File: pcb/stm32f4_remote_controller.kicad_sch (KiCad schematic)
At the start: 0 parts

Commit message: pcb: add source supply
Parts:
- added C1, C2, C3, C4, C5, C7: 100n, symbol Device:C
- added C6: 10u, symbol Device:C
- added C8, C9: 20p, symbol Device:C
- added J1: Conn_01x04_Pin, symbol Connector:Conn_01x04_Pin
- added U1: STM32F401CCU6, Package_DFN_QFN:QFN-48-1EP_7x7mm_P0.5mm_EP5.6x5.6mm, symbol MCU_ST_STM32F4:STM32F401CCUx
- added Y1: 8Mhz, symbol Device:Crystal_GND24
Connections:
- new net +STEP_UP_3.3V: C1.1, C2.1, C3.1, C4.1, C5.1, C6.1, J1.1 (Pin_1), U1.1 (VBAT), U1.24 (VDD), U1.36 (VDD), U1.48 (VDD)
- new net GND: C1.2, C2.2, C3.2, C4.2, C5.2, C6.2, C7.2, C8.2, C9.2, J1.4 (Pin_4), U1.23 (VSS), U1.35 (VSS), U1.44 (BOOT0), U1.47 (VSS), U1.49 (VSS), U1.8 (VSSA), Y1.2, Y1.4
- new net HSE_IN: C9.1, U1.5 (PH0), Y1.1
- new net HSE_OUT: C8.1, U1.6 (PH1), Y1.3
- new net NRST: C7.1, U1.7 (NRST)
- new net SWCLK: J1.3 (Pin_3), U1.37 (PA14)
- new net SWDIO: J1.2 (Pin_2), U1.34 (PA13)

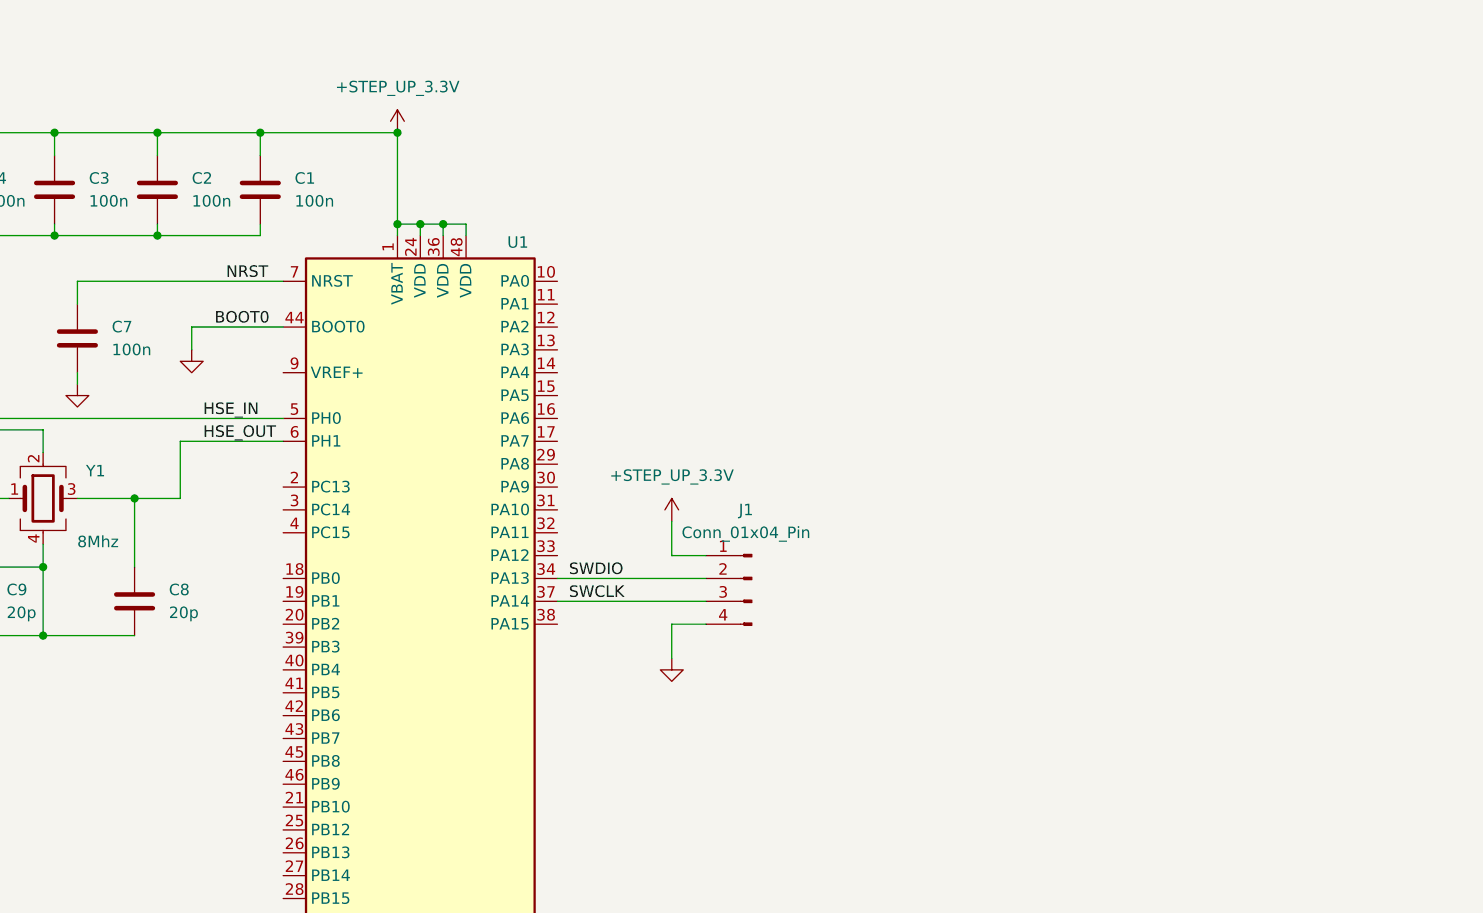
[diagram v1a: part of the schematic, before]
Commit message: pcb: add oled to sch
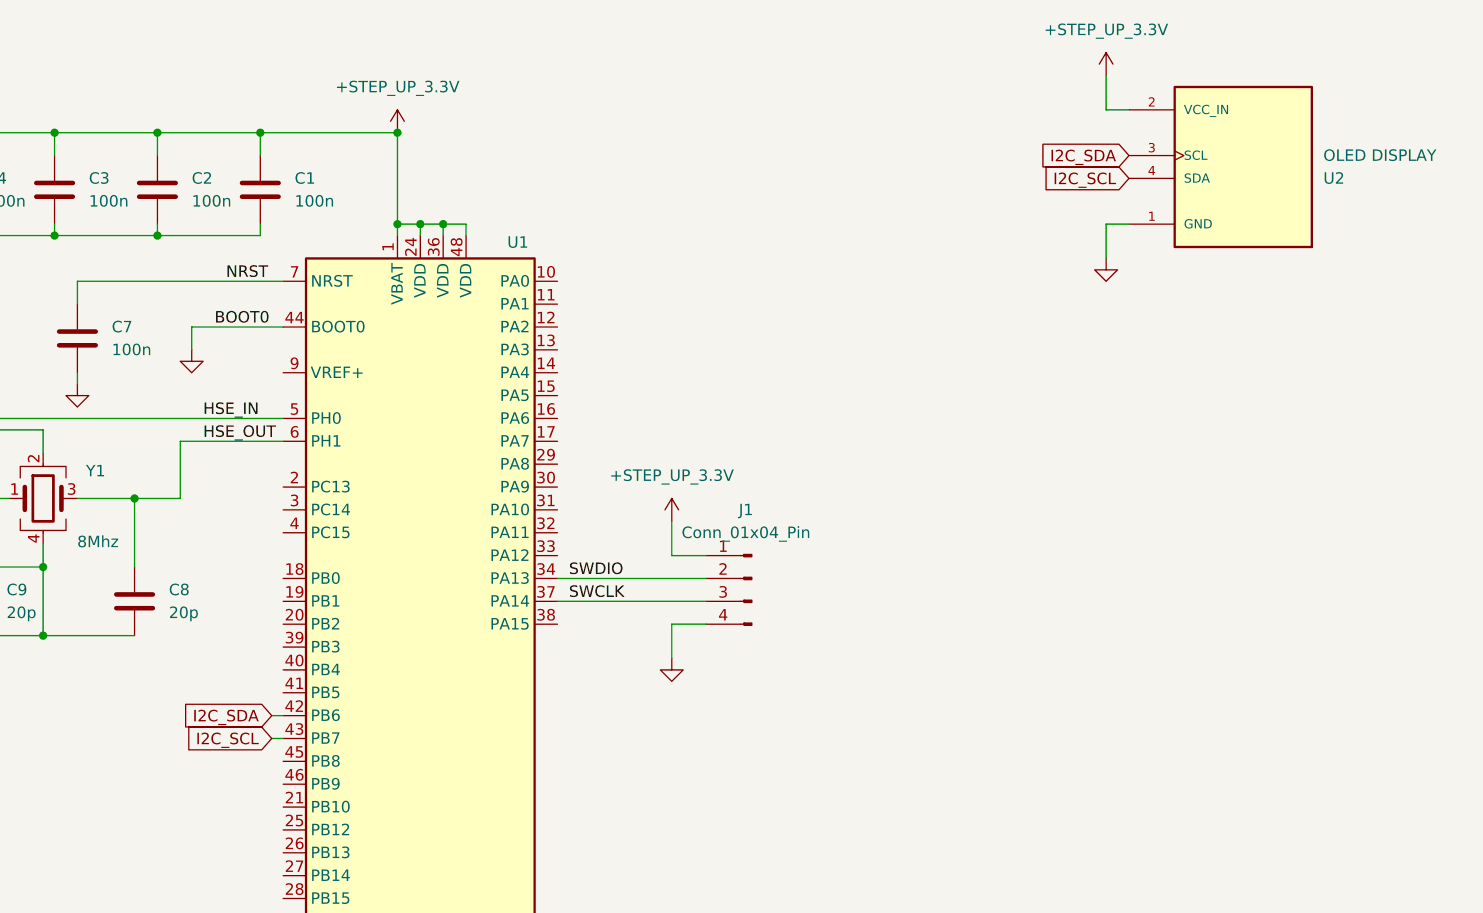
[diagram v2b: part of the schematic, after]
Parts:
- added U2: OLED DISPLAY, DM-OLED096-636:MODULE_DM-OLED096-636, symbol DM-OLED096-636:DM-OLED096-636
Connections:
- net +STEP_UP_3.3V: now also U2.2 (VCC_IN)
- net GND: now also U2.1 (GND)
- net I2C_SDA: now reaches U1.42 (PB6)
- net I2C_SDA: now also U2.3 (SCL)
- net I2C_SCL: now reaches U1.43 (PB7)
- net I2C_SCL: now also U2.4 (SDA)

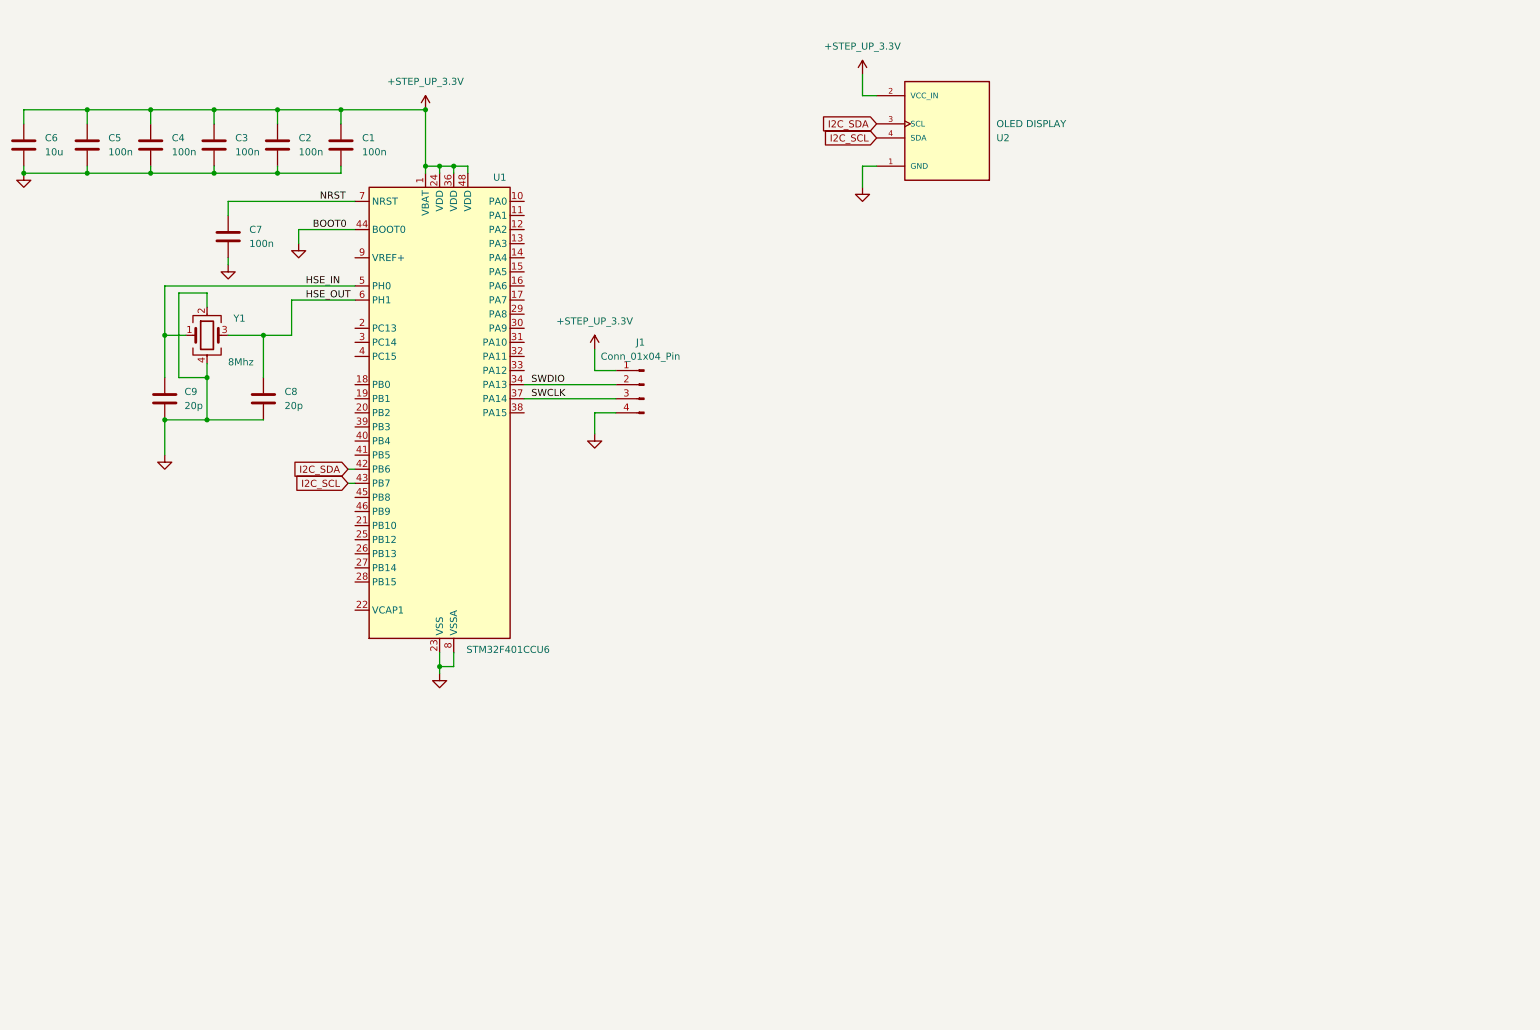
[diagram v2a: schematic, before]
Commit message: pcb: add hm-10 sch
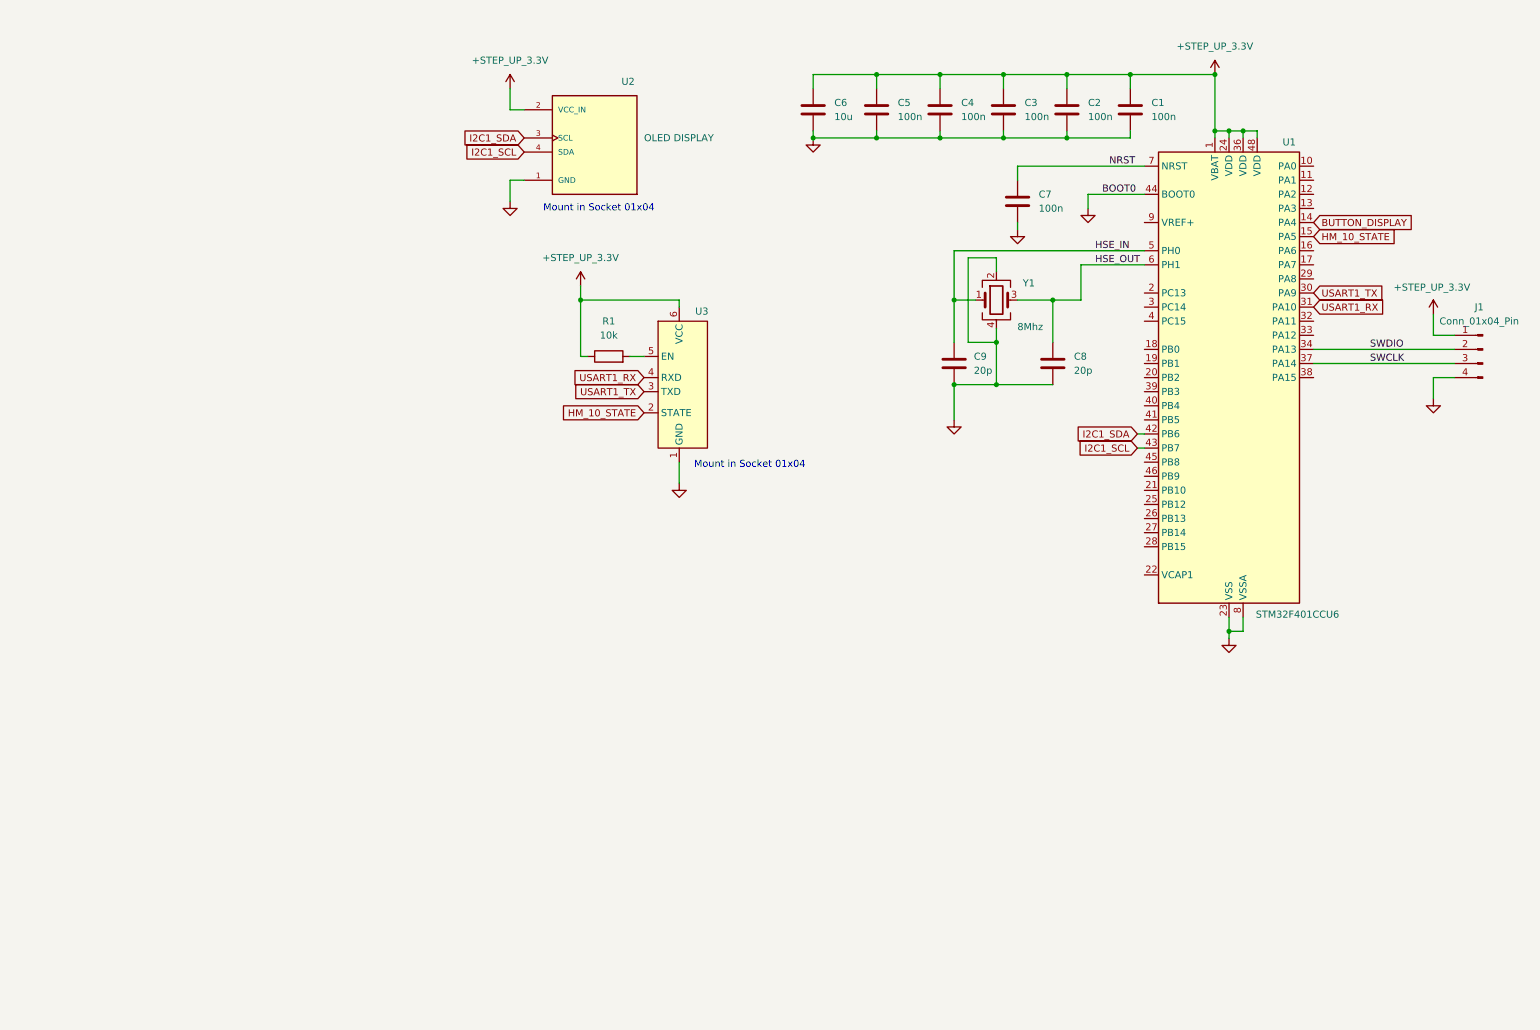
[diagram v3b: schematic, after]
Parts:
- added R1: 10k, symbol Device:R
- added U3: ~, symbol hm-10:hm-10
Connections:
- net +STEP_UP_3.3V: now also R1.1, U3.6 (VCC)
- net GND: now also U3.1 (GND)
- net BUTTON_DISPLAY: now reaches U1.14 (PA4)
- net HM_10_STATE: now reaches U1.15 (PA5)
- net HM_10_STATE: now also U3.2 (STATE)
- net USART1_TX: now reaches U1.30 (PA9)
- net USART1_TX: now also U3.3 (TXD)
- net USART1_RX: now reaches U1.31 (PA10)
- net USART1_RX: now also U3.4 (RXD)
- net I2C_SCL renamed I2C1_SCL
- net I2C_SDA renamed I2C1_SDA
- new net: R1.2, U3.5 (EN)
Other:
- note added: "Mount in Socket 01x04"
- moved on the sheet: C1, C2, C3, C4, C5, C6, C7, C8, C9, J1, U1, U2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

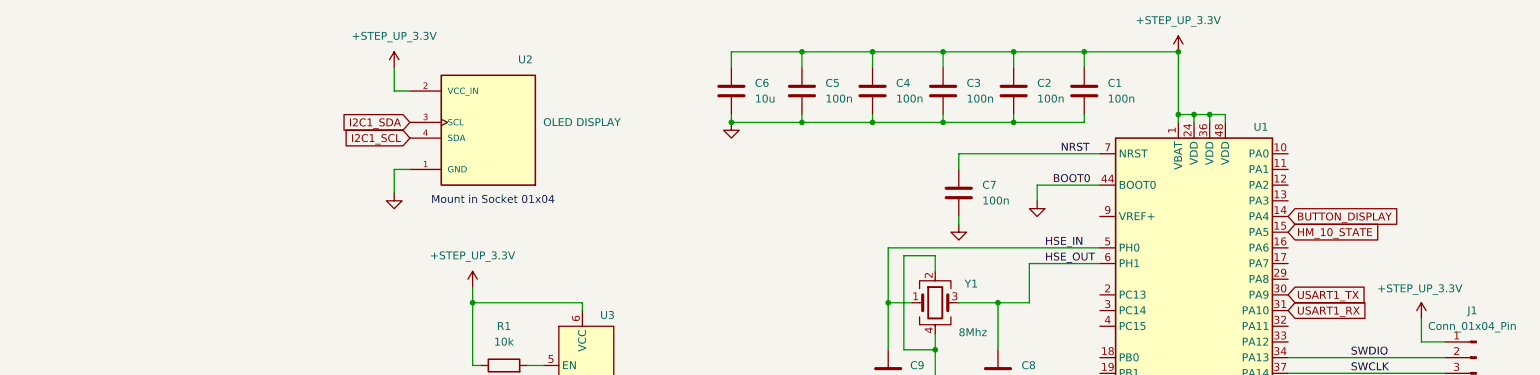
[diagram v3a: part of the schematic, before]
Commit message: pcb: add button debounce circuit
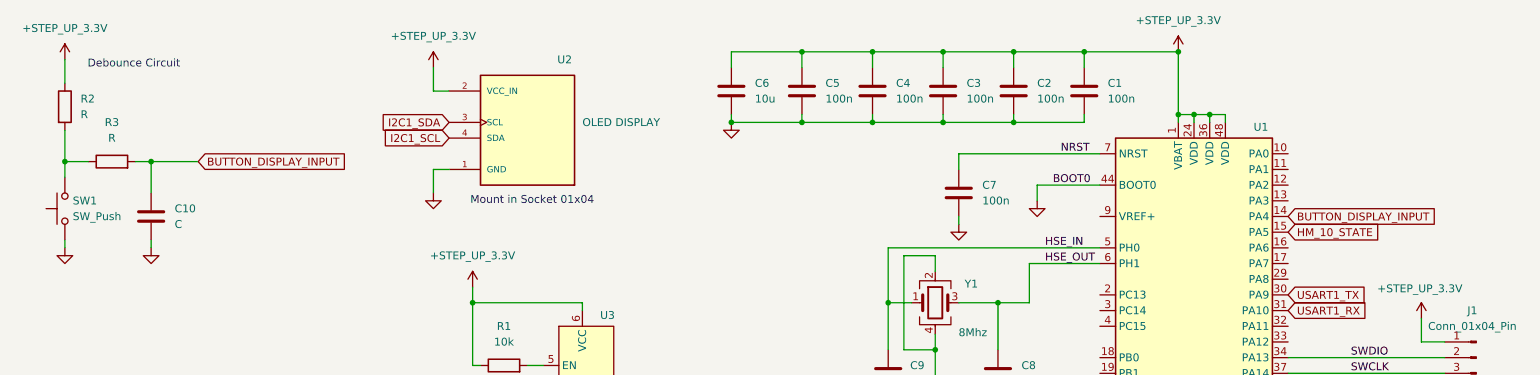
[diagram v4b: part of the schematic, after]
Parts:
- added C10: C, symbol Device:C
- added R2, R3: R, symbol Device:R
- added SW1: SW_Push, symbol Switch:SW_Push
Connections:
- net +STEP_UP_3.3V: now also R2.1
- net GND: now also C10.2, SW1.1
- net BUTTON_DISPLAY renamed BUTTON_DISPLAY_INPUT
- net BUTTON_DISPLAY_INPUT: now also C10.1, R3.2
- new net: R2.2, R3.1, SW1.2
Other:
- note added: "Debounce Circuit"
- moved on the sheet: U2
